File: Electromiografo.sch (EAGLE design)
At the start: 38 parts, among them IC1 ESP32-S3-WROOM-1-N16R8, IC2 MCP73831T-2DCI_OT, IC3 741G3157DBVR, IC4 LP38692MP-3.3_NOPB, IC5 REF2033AIDDCT, IC6 LMV321IDBVRG4, IC7 LMV321IDBVRG4, IC8 LMV321IDBVRG4, IC9 AD8223ARMZ, J1 1981584-1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

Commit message: modificaciones terminadas
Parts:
- added IC10: LMV321IDBVRG4, SamacSys_Parts:LMV321IDBVRG4
- added R12, R13: (no value), rcl:R-EU_R0805
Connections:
- removed net N$13: J1.4
- new net N$17: IC10.1IN-, R12.1, R13.1
- new net N$18: IC10.OUT, R12.2
- net +3V3: now also IC10.VCC+
- net GND: now also IC10.GND, R13.2
- net N$38: now also IC10.1IN+
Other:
- note added: "1. Agregar un amplificador driver (antes del adc)(listo) 2. Agregar el REF2033(listo) 3. Definir cuales son los pines D+ y D- del USB-C(listo) 4. Invertir el conector de la OLED(listo) 5. Reemplazar el ESP32 por un ESP32-S3(listo) 6. Verificar el SW(listo)"
- note added: "OUTADC"
- note removed: "1. Agregar un amplificador driver (antes del adc) 2. Agregar el REF2033(listo) 3. Definir cuales son los pines D+ y D- del USB-C 4. Invertir el conector de la OLED(listo) 5. Reemplazar el ESP32 por un ESP32-S3(listo) 6. Verificar el SW(listo)"
- note removed: "FILTRO PASA BAJO"
- note removed: "OUT ADC"
- moved on the sheet: C10, C5, C6, C7, C8, C9, IC6, IC7, IC8, R10, R5, R6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

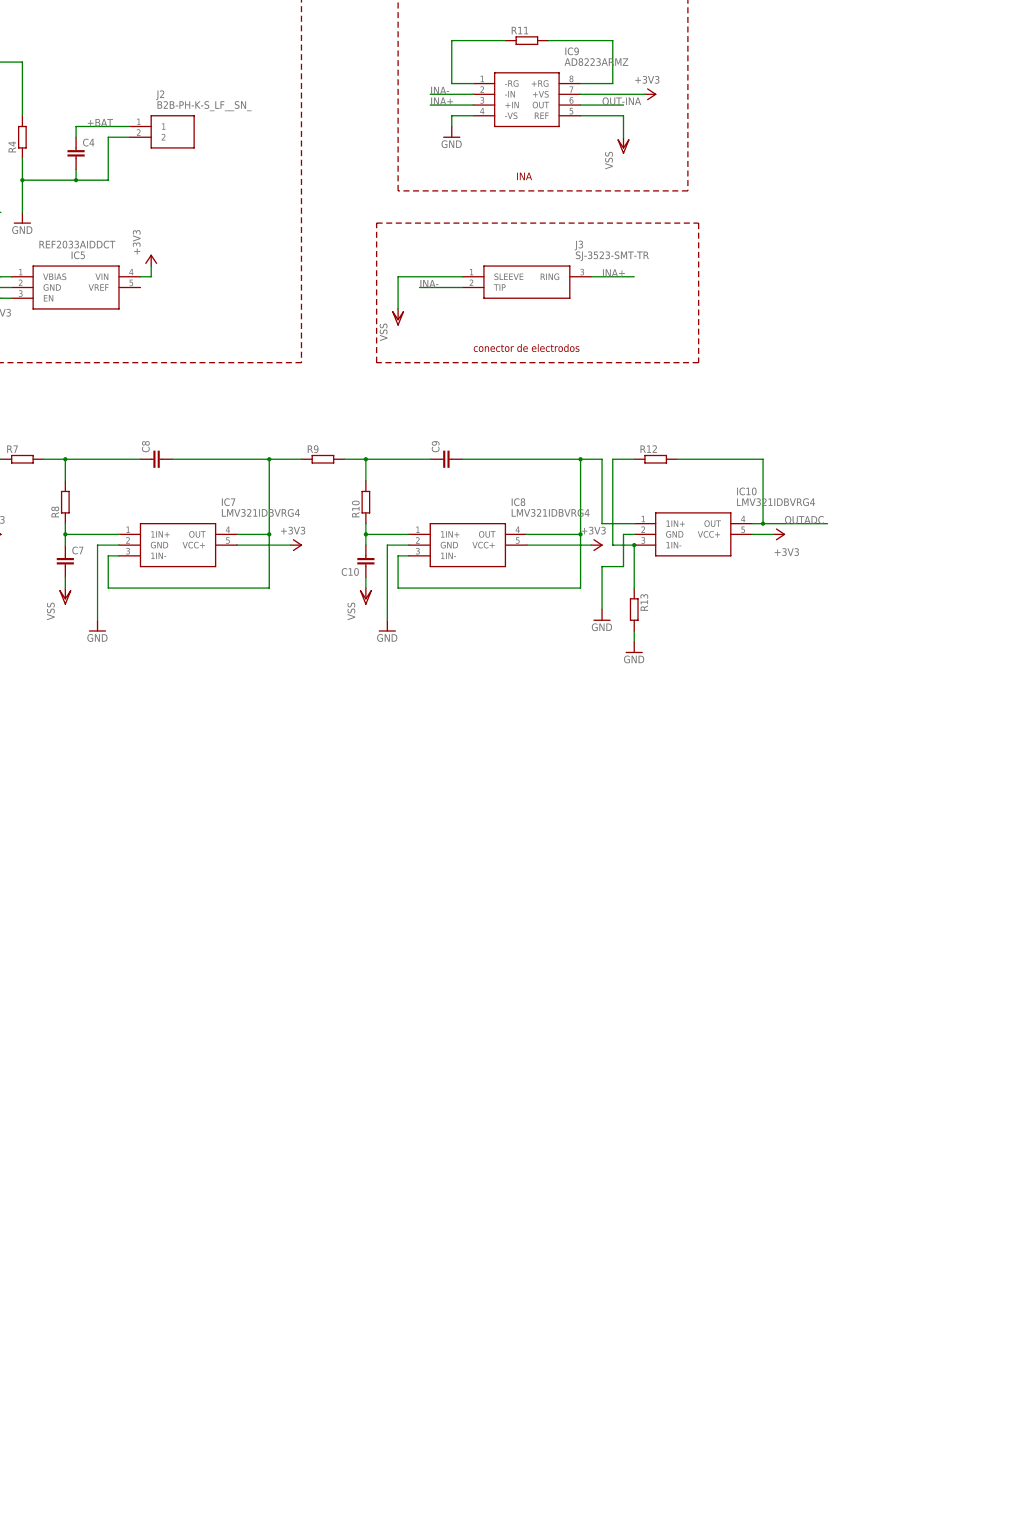
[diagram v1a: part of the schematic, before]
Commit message: Se remplazo conector de bateria
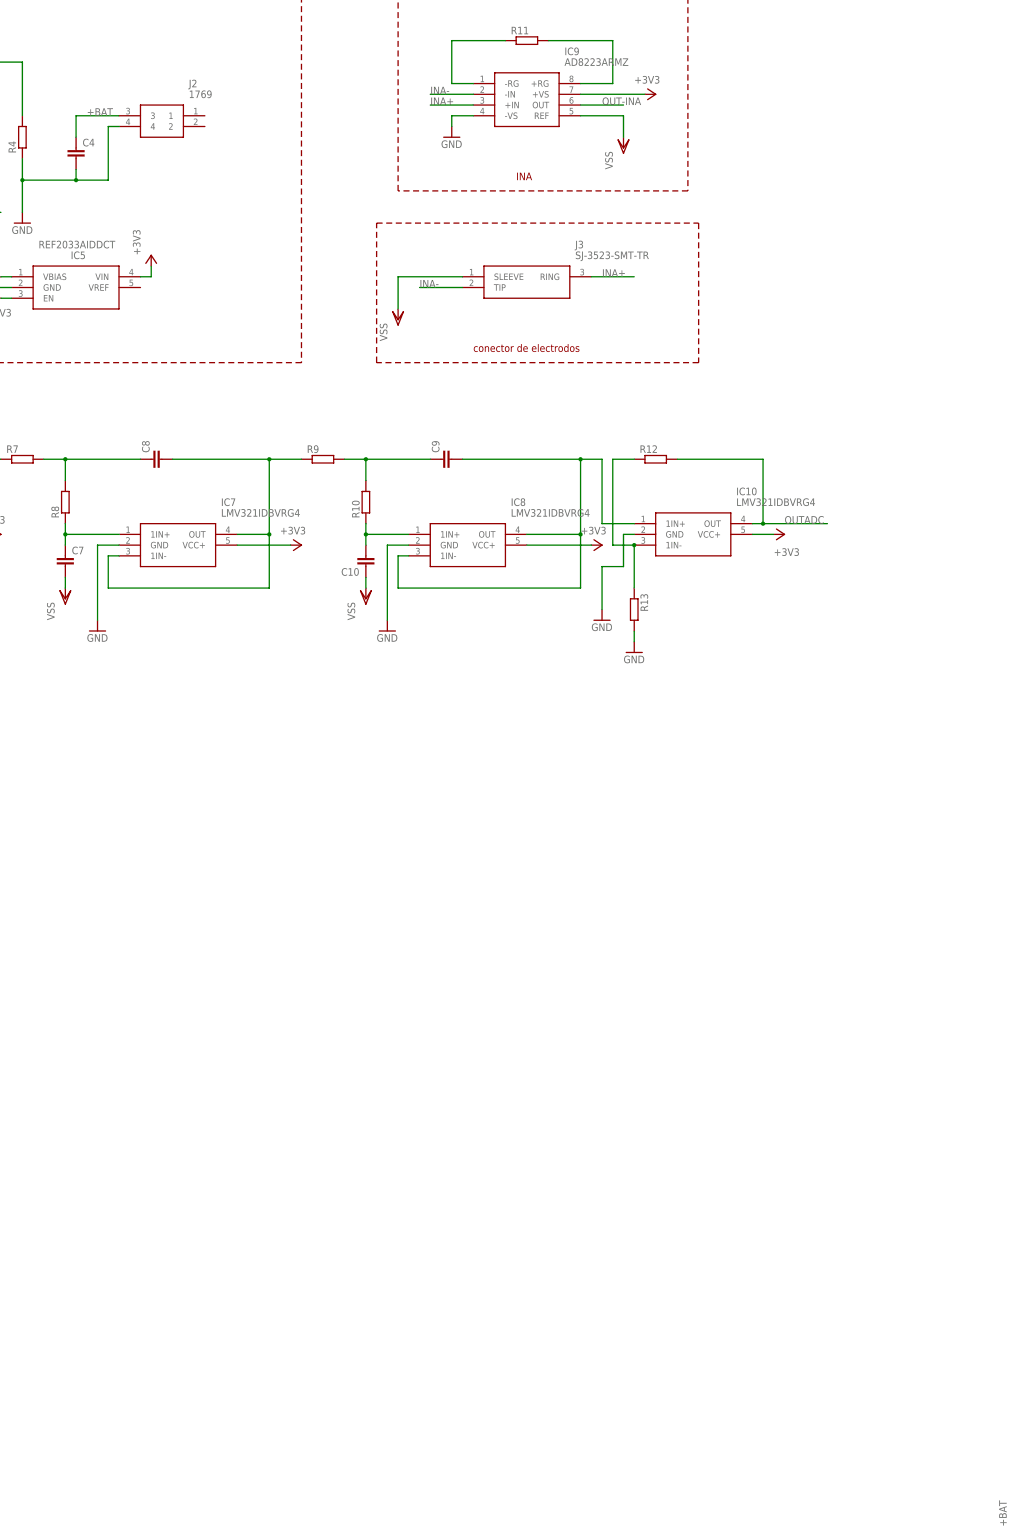
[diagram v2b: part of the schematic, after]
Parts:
- J2: value B2B-PH-K-S_LF__SN_ -> 1769; device SamacSys_Parts:B2B-PH-K-S_LF__SN_ -> SamacSys_Parts:1769
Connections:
- net +BAT: now also J2.3; no longer J2.1
- net GND: now also J2.4; no longer J2.2
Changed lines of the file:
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@@
 <part name="R4" library="rcl" library_urn="urn:adsk.eagle:library:334" deviceset="R-EU_" device="R0805" package3d_urn="urn:adsk.eagle:package:23553/2"/>
 <part name="LED1" library="PulseOximeterECG_AU" library_urn="urn:adsk.eagle:library:14846661" deviceset="LED" device="CHIP-LED0805" package3d_urn="urn:adsk.eagle:package:14846712/2"/>
-<part name="J2" library="SamacSys_Parts" deviceset="B2B-PH-K-S_LF__SN_" device=""/>
 <part name="GND10" library="supply1" library_urn="urn:adsk.eagle:library:371" deviceset="GND" device=""/>
 <part name="P+2" library="supply1" library_urn="urn:adsk.eagle:library:371" deviceset="+5V" device=""/>
@@
 <part name="+3V12" library="supply1" library_urn="urn:adsk.eagle:library:371" deviceset="+3V3" device=""/>
 <part name="GND18" library="PulseOximeterECG_AU" library_urn="urn:adsk.eagle:library:14846661" deviceset="GND" device=""/>
+<part name="J2" library="SamacSys_Parts" deviceset="1769" device=""/>
 </parts>
 <sheets>
@@
 <attribute name="VALUE" x="302.895" y="196.088" size="1.778" layer="96" rot="R90"/>
 </instance>
-<instance part="J2" gate="G$1" x="350.52" y="198.12" smashed="yes">
-<attribute name="NAME" x="356.87" y="205.74" size="1.778" layer="95" align="center-left"/>
-<attribute name="VALUE" x="356.87" y="203.2" size="1.778" layer="96" align="center-left"/>
-</instance>
 <instance part="GND10" gate="1" x="325.12" y="175.26" smashed="yes">
 <attribute name="VALUE" x="322.58" y="172.72" size="1.778" layer="96"/>
@@
 <instance part="GND18" gate="1" x="462.28" y="81.28" smashed="yes" grouprefs="FILTRO">
 <attribute name="VALUE" x="459.74" y="78.74" size="1.778" layer="96"/>
+</instance>
+<instance part="J2" gate="G$1" x="347.98" y="200.66" smashed="yes">
+<attribute name="NAME" x="364.49" y="208.28" size="1.778" layer="95" align="center-left"/>
+<attribute name="VALUE" x="364.49" y="205.74" size="1.778" layer="96" align="center-left"/>
 </instance>
 </instances>
@@
 <wire x1="337.82" y1="185.42" x2="345.44" y2="185.42" width="0.1524" layer="91"/>
 <junction x="337.82" y="185.42"/>
-<pinref part="J2" gate="G$1" pin="2"/>
-<wire x1="345.44" y1="185.42" x2="345.44" y2="195.58" width="0.1524" layer="91"/>
-<wire x1="345.44" y1="195.58" x2="350.52" y2="195.58" width="0.1524" layer="91"/>
+<wire x1="345.44" y1="185.42" x2="345.44" y2="198.12" width="0.1524" layer="91"/>
 <pinref part="GND10" gate="1" pin="GND"/>
 <wire x1="325.12" y1="177.8" x2="325.12" y2="185.42" width="0.1524" layer="91"/>
 <junction x="325.12" y="185.42"/>
+<pinref part="J2" gate="G$1" pin="4"/>
+<wire x1="347.98" y1="198.12" x2="345.44" y2="198.12" width="0.1524" layer="91"/>
 </segment>
 <segment>
@@
 <segment>
 <pinref part="C4" gate="G$1" pin="1"/>
-<pinref part="J2" gate="G$1" pin="1"/>
-<wire x1="337.82" y1="195.58" x2="337.82" y2="198.12" width="0.1524" layer="91"/>
-<wire x1="337.82" y1="198.12" x2="350.52" y2="198.12" width="0.1524" layer="91"/>
-<label x="340.36" y="198.12" size="1.778" layer="95"/>
-</segment>
-</net>
+<label x="340.36" y="200.66" size="1.778" layer="95"/>
+<pinref part="J2" gate="G$1" pin="3"/>
+<wire x1="347.98" y1="200.66" x2="337.82" y2="200.66" width="0.1524" layer="91"/>
+<wire x1="337.82" y1="200.66" x2="337.82" y2="195.58" width="0.1524" layer="91"/>
+</segment>
+<segment>
+<label x="556.26" y="-127" size="1.778" layer="95" rot="R270"/>
+</segment>
+</net>

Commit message: Se ruteo las pistas de INA, Filtro y conector de electrodos
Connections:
- removed net N$18: IC10.OUT, R12.2
- removed net N$3: IC1.IO7
- new net OUTADC: IC1.IO7, IC10.OUT, R12.2
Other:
- note removed: "OUTADC"
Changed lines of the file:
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@@
 <plain>
 <text x="203.2" y="144.78" size="1.778" layer="95" rot="R90" grouprefs="SP32">FLASH</text>
-<text x="109.22" y="157.48" size="1.778" layer="95" grouprefs="SP32">OUTADC</text>
 <text x="109.22" y="149.86" size="1.778" layer="95" grouprefs="SP32">DAC1</text>
 <text x="109.22" y="147.32" size="1.778" layer="95" grouprefs="SP32">DAC2</text>
@@
 6. Verificar el SW(listo)</text>
 <text x="368.3" y="248.92" size="1.778" layer="94">7. Verificar el conector JST de la bateria</text>
-<text x="505.46" y="104.14" size="1.778" layer="95">OUTADC</text>
 </plain>
 <instances>
@@
 </segment>
 </net>
-<net name="N$3" class="0">
+<net name="OUTADC" class="0">
 <segment>
 <wire x1="127" y1="157.48" x2="106.68" y2="157.48" width="0.1524" layer="91" grouprefs="SP32"/>
 <pinref part="IC1" gate="G$1" pin="IO7"/>
+<label x="109.22" y="157.48" size="1.778" layer="95"/>
+</segment>
+<segment>
+<pinref part="R12" gate="G$1" pin="2"/>
+<wire x1="480.06" y1="119.38" x2="500.38" y2="119.38" width="0.1524" layer="91" grouprefs="FILTRO"/>
+<wire x1="500.38" y1="119.38" x2="500.38" y2="104.14" width="0.1524" layer="91" grouprefs="FILTRO"/>
+<pinref part="IC10" gate="G$1" pin="OUT"/>
+<wire x1="500.38" y1="104.14" x2="497.84" y2="104.14" width="0.1524" layer="91" grouprefs="FILTRO"/>
+<wire x1="500.38" y1="104.14" x2="513.08" y2="104.14" width="0.1524" layer="91"/>
+<junction x="500.38" y="104.14"/>
+<label x="505.46" y="104.14" size="1.778" layer="95"/>
 </segment>
 </net>
@@
 </segment>
 </net>
-<net name="N$18" class="0">
-<segment>
-<pinref part="R12" gate="G$1" pin="2"/>
-<wire x1="480.06" y1="119.38" x2="500.38" y2="119.38" width="0.1524" layer="91" grouprefs="FILTRO"/>
-<wire x1="500.38" y1="119.38" x2="500.38" y2="104.14" width="0.1524" layer="91" grouprefs="FILTRO"/>
-<pinref part="IC10" gate="G$1" pin="OUT"/>
-<wire x1="500.38" y1="104.14" x2="497.84" y2="104.14" width="0.1524" layer="91" grouprefs="FILTRO"/>
-<wire x1="500.38" y1="104.14" x2="515.62" y2="104.14" width="0.1524" layer="91"/>
-<junction x="500.38" y="104.14"/>
-</segment>
-</net>

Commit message: modificacion pulsadores
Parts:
- S1, S2: value PTS125SM73SMTR21M_LFS -> B3U-1000PM; device SamacSys_Parts:PTS125SM73SMTR21M_LFS -> SamacSys_Parts:B3U-1000PM
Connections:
- net GND: now also S1.COM, S2.NO; no longer S1.COM_2, S2.NO_2
- net N$1: now also S1.NO; no longer S1.NO_2
- net N$2: now also S2.COM; no longer S2.COM_2
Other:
- note added: "RESET"
- note added: "flash"
- note removed: "FLASH"
- note removed: "REST"
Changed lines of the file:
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@@
 <parts>
 <part name="GND1" library="supply1" library_urn="urn:adsk.eagle:library:371" deviceset="GND" device=""/>
-<part name="S1" library="SamacSys_Parts" deviceset="PTS125SM73SMTR21M_LFS" device=""/>
 <part name="R1" library="rcl" library_urn="urn:adsk.eagle:library:334" deviceset="R-EU_" device="R0805" package3d_urn="urn:adsk.eagle:package:23553/2" value="10K"/>
 <part name="GND2" library="supply1" library_urn="urn:adsk.eagle:library:371" deviceset="GND" device=""/>
@@
 <part name="+3V3" library="PulseOximeterECG_AU" library_urn="urn:adsk.eagle:library:14846661" deviceset="+3V3" device=""/>
 <part name="GND4" library="PulseOximeterECG_AU" library_urn="urn:adsk.eagle:library:14846661" deviceset="GND" device=""/>
-<part name="S2" library="SamacSys_Parts" deviceset="PTS125SM73SMTR21M_LFS" device=""/>
 <part name="C2" library="rcl" library_urn="urn:adsk.eagle:library:334" deviceset="C-EU" device="C0603" package3d_urn="urn:adsk.eagle:package:23616/2" value="0.1U"/>
 <part name="JP1" library="pinhead" library_urn="urn:adsk.eagle:library:325" deviceset="PINHD-1X4" device="/90" package3d_urn="urn:adsk.eagle:package:22404/2"/>
@@
 <part name="GND18" library="PulseOximeterECG_AU" library_urn="urn:adsk.eagle:library:14846661" deviceset="GND" device=""/>
 <part name="J2" library="SamacSys_Parts" deviceset="1769" device=""/>
+<part name="S1" library="SamacSys_Parts" deviceset="B3U-1000PM" device=""/>
+<part name="S2" library="SamacSys_Parts" deviceset="B3U-1000PM" device=""/>
 </parts>
 <sheets>
 <sheet>
 <plain>
-<text x="203.2" y="144.78" size="1.778" layer="95" rot="R90" grouprefs="SP32">FLASH</text>
 <text x="109.22" y="149.86" size="1.778" layer="95" grouprefs="SP32">DAC1</text>
 <text x="109.22" y="147.32" size="1.778" layer="95" grouprefs="SP32">DAC2</text>
@@
 <text x="167.64" y="144.78" size="1.778" layer="95" grouprefs="SP32">TX</text>
 <text x="167.64" y="147.32" size="1.778" layer="95" grouprefs="SP32">RX</text>
-<text x="93.98" y="134.62" size="1.778" layer="95" rot="R90" grouprefs="SP32">REST</text>
 <text x="91.44" y="165.1" size="1.778" layer="95" grouprefs="SP32">RESET32</text>
 <text x="187.96" y="86.36" size="1.778" layer="95" rot="MR0" grouprefs="IMAGEN">OLED</text>
@@
 6. Verificar el SW(listo)</text>
 <text x="368.3" y="248.92" size="1.778" layer="94">7. Verificar el conector JST de la bateria</text>
+<text x="203.2" y="152.4" size="1.778" layer="95" rot="R270">flash</text>
+<text x="93.98" y="134.62" size="1.778" layer="95" rot="R90">RESET</text>
 </plain>
 <instances>
@@
 <attribute name="VALUE" x="162.56" y="104.14" size="1.778" layer="96"/>
 </instance>
-<instance part="S1" gate="G$1" x="195.58" y="134.62" smashed="yes" rot="R90" grouprefs="SP32">
-<attribute name="NAME" x="187.96" y="140.97" size="1.778" layer="95" rot="R90" align="center-left"/>
-</instance>
 <instance part="R1" gate="G$1" x="195.58" y="193.04" smashed="yes" rot="R90" grouprefs="SP32">
 <attribute name="NAME" x="191.5414" y="191.77" size="1.778" layer="95" rot="R90"/>
@@
 <attribute name="VALUE" x="71.12" y="137.16" size="1.778" layer="96"/>
 </instance>
-<instance part="S2" gate="G$1" x="86.36" y="121.92" smashed="yes" rot="R90" grouprefs="SP32">
-<attribute name="NAME" x="81.28" y="130.81" size="1.778" layer="95" rot="R90" align="center-left"/>
-</instance>
 <instance part="C2" gate="G$1" x="78.74" y="167.64" smashed="yes" rot="R90" grouprefs="SP32">
 <attribute name="NAME" x="78.359" y="169.164" size="1.778" layer="95" rot="R90"/>
@@
 <attribute name="NAME" x="364.49" y="208.28" size="1.778" layer="95" align="center-left"/>
 <attribute name="VALUE" x="364.49" y="205.74" size="1.778" layer="96" align="center-left"/>
+</instance>
+<instance part="S1" gate="G$1" x="195.58" y="162.56" smashed="yes" rot="MR270">
+<attribute name="NAME" x="187.96" y="151.13" size="1.778" layer="95" rot="MR270" align="center-left"/>
+<attribute name="VALUE" x="190.5" y="153.67" size="1.778" layer="96" rot="MR270" align="center-left"/>
+</instance>
+<instance part="S2" gate="G$1" x="86.36" y="149.86" smashed="yes" rot="MR270">
+<attribute name="NAME" x="78.74" y="140.97" size="1.778" layer="95" rot="MR270" align="center-left"/>
+<attribute name="VALUE" x="81.28" y="140.97" size="1.778" layer="96" rot="MR270" align="center-left"/>
 </instance>
 </instances>
@@
 <net name="GND" class="0">
 <segment>
-<pinref part="S1" gate="G$1" pin="COM_2"/>
-<wire x1="198.12" y1="165.1" x2="198.12" y2="172.72" width="0.1524" layer="91" grouprefs="SP32"/>
 <wire x1="198.12" y1="172.72" x2="208.28" y2="172.72" width="0.1524" layer="91" grouprefs="SP32"/>
 <pinref part="GND2" gate="1" pin="GND"/>
@@
 <wire x1="205.74" y1="180.34" x2="208.28" y2="180.34" width="0.1524" layer="91"/>
 <wire x1="208.28" y1="180.34" x2="208.28" y2="172.72" width="0.1524" layer="91"/>
+<pinref part="S1" gate="G$1" pin="COM"/>
+<wire x1="198.12" y1="162.56" x2="198.12" y2="172.72" width="0.1524" layer="91"/>
+<junction x="198.12" y="172.72"/>
 </segment>
 <segment>
@@
 </segment>
 <segment>
-<pinref part="S2" gate="G$1" pin="NO_2"/>
-<wire x1="86.36" y1="152.4" x2="86.36" y2="157.48" width="0.1524" layer="91" grouprefs="SP32"/>
 <pinref part="GND4" gate="1" pin="GND"/>
 <wire x1="86.36" y1="157.48" x2="73.66" y2="157.48" width="0.1524" layer="91" grouprefs="SP32"/>
@@
 <wire x1="73.66" y1="167.64" x2="73.66" y2="157.48" width="0.1524" layer="91" grouprefs="SP32"/>
 <junction x="73.66" y="157.48" grouprefs="SP32"/>
+<pinref part="S2" gate="G$1" pin="NO"/>
+<wire x1="86.36" y1="149.86" x2="86.36" y2="157.48" width="0.1524" layer="91"/>
 </segment>
 <segment>
@@
 <wire x1="160.02" y1="172.72" x2="195.58" y2="172.72" width="0.1524" layer="91" grouprefs="SP32"/>
 <wire x1="195.58" y1="172.72" x2="195.58" y2="180.34" width="0.1524" layer="91" grouprefs="SP32"/>
-<pinref part="S1" gate="G$1" pin="NO_2"/>
 <wire x1="195.58" y1="180.34" x2="195.58" y2="187.96" width="0.1524" layer="91" grouprefs="SP32"/>
-<wire x1="195.58" y1="172.72" x2="195.58" y2="165.1" width="0.1524" layer="91" grouprefs="SP32"/>
-<junction x="195.58" y="172.72" grouprefs="SP32"/>
 <pinref part="C11" gate="G$1" pin="1"/>
 <wire x1="198.12" y1="180.34" x2="195.58" y2="180.34" width="0.1524" layer="91"/>
 <junction x="195.58" y="180.34"/>
 <pinref part="IC1" gate="G$1" pin="IO45"/>
+<pinref part="S1" gate="G$1" pin="NO"/>
+<wire x1="195.58" y1="162.56" x2="195.58" y2="172.72" width="0.1524" layer="91"/>
+<junction x="195.58" y="172.72"/>
 </segment>
 </net>
@@
 <wire x1="88.9" y1="167.64" x2="127" y2="167.64" width="0.1524" layer="91" grouprefs="SP32"/>
 <junction x="88.9" y="167.64" grouprefs="SP32"/>
-<pinref part="S2" gate="G$1" pin="COM_2"/>
-<wire x1="88.9" y1="152.4" x2="88.9" y2="167.64" width="0.1524" layer="91" grouprefs="SP32"/>
 <pinref part="C2" gate="G$1" pin="2"/>
 <wire x1="83.82" y1="167.64" x2="88.9" y2="167.64" width="0.1524" layer="91" grouprefs="SP32"/>
 <pinref part="IC1" gate="G$1" pin="EN"/>
+<pinref part="S2" gate="G$1" pin="COM"/>
+<wire x1="88.9" y1="149.86" x2="88.9" y2="167.64" width="0.1524" layer="91"/>
 </segment>
 </net>
